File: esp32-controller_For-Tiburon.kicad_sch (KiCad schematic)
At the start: 6 parts, among them J1 Conn_01x02_Pin, J2 Conn_01x02_Pin, J3 SD_Card_Receptacle, J5 Conn_01x04_Pin, J6 Conn_01x02_Pin, U1 ESP32-S3-WROOM-1

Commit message: test push
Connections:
- net at U1.14 (USB_D+): now also J2.1 (Pin_1)
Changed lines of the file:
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@@
 	(generator_version "9.0")
 	(paper "A4")
+	(wire
+		(pts
+			(xy 171.45 87.63) (xy 156.21 87.63)
+		)
+		(stroke
+			(width 0)
+			(type default)
+		)
+	)
+	(wire
+		(pts
+			(xy 171.45 99.06) (xy 171.45 87.63)
+		)
+		(stroke
+			(width 0)
+			(type default)
+		)
+	)
 	(symbol
 		(lib_id "Connector:Conn_01x02_Pin")

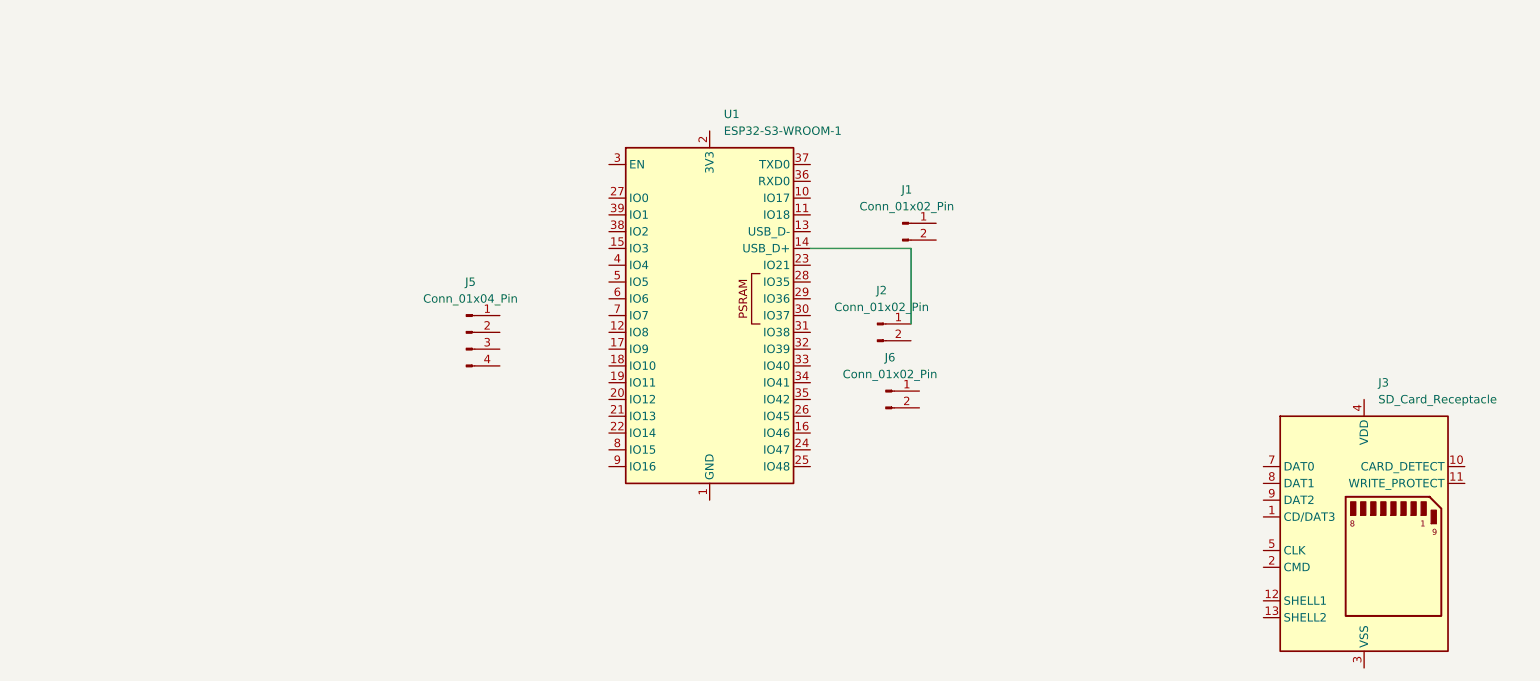
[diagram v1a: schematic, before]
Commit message: added power pin
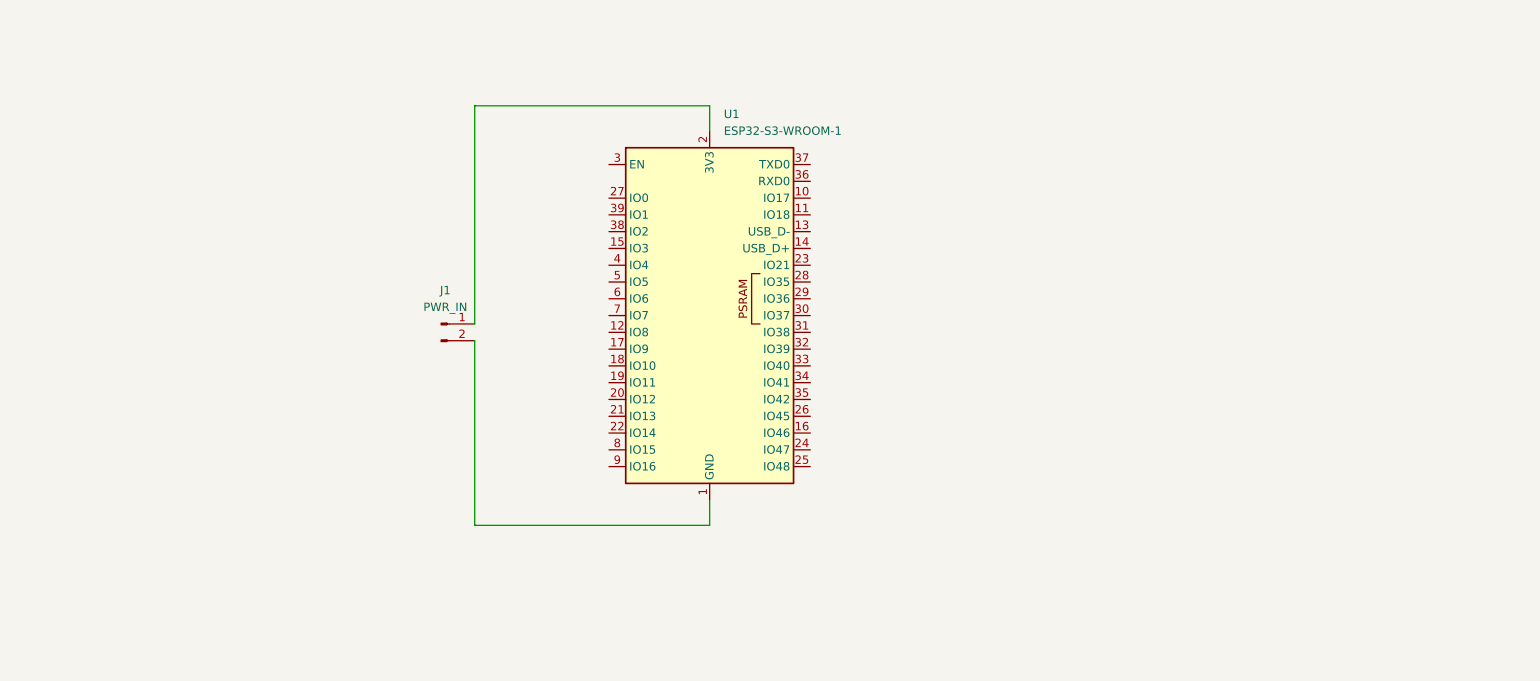
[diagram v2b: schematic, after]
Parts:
- removed J2, J6: Conn_01x02_Pin, symbol Connector:Conn_01x02_Pin
- removed J3: SD_Card_Receptacle, symbol Connector:SD_Card_Receptacle
- removed J5: Conn_01x04_Pin, symbol Connector:Conn_01x04_Pin
- J1: value Conn_01x02_Pin -> PWR_IN
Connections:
- net at J1.1 (Pin_1): now also U1.2 (3V3)
- net at J1.2 (Pin_2): now also U1.1 (GND), U1.40 (GND), U1.41 (GND)

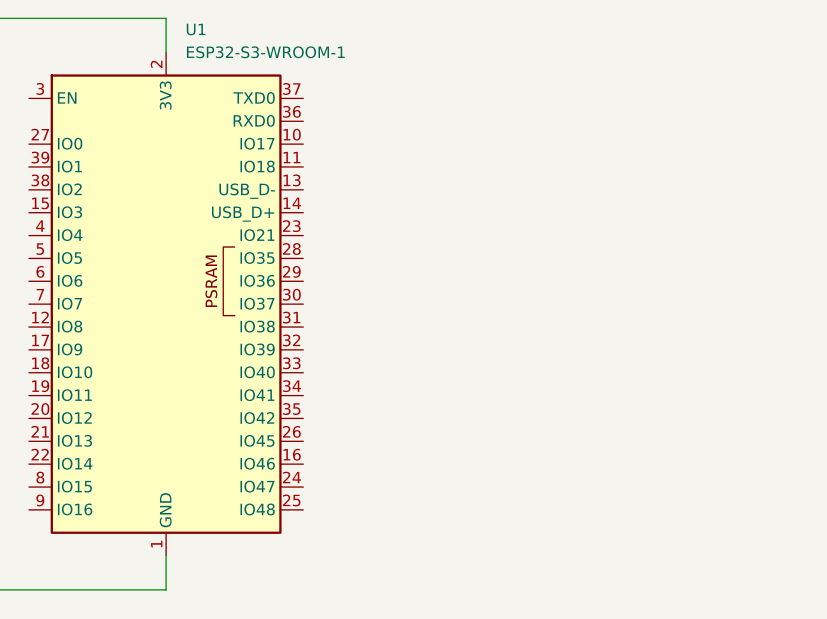
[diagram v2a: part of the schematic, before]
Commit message: added uart pins
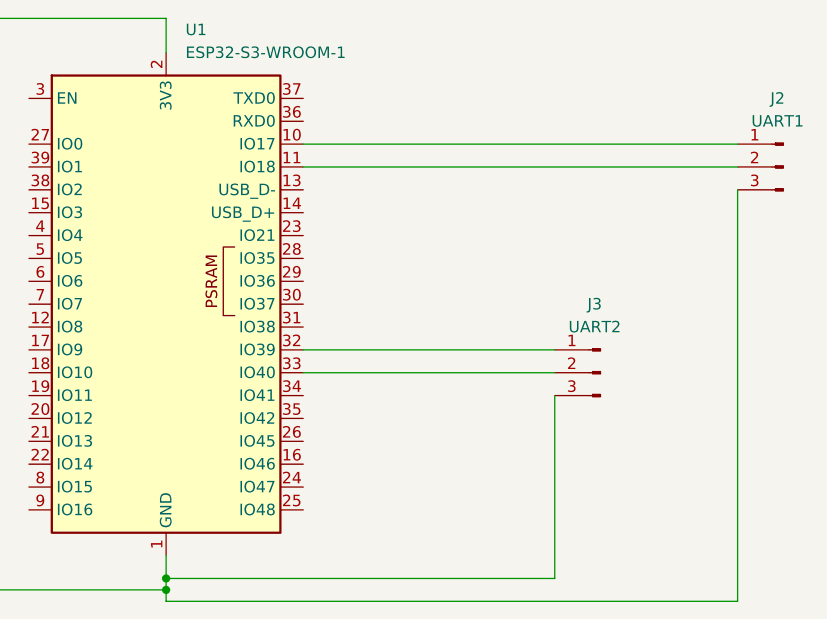
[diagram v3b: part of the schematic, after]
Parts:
- added J2: UART1, symbol Connector:Conn_01x03_Pin
- added J3: UART2, symbol Connector:Conn_01x03_Pin
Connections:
- net at J1.2 (Pin_2), U1.1 (GND), U1.40 (GND)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: now also J2.3 (Pin_3), J3.3 (Pin_3)
- net at U1.10 (IO17): now also J2.1 (Pin_1)
- net at U1.11 (IO18): now also J2.2 (Pin_2)
- net at U1.32 (IO39): now also J3.1 (Pin_1)
- net at U1.33 (IO40): now also J3.2 (Pin_2)
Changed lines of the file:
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@@
 	(generator_version "9.0")
 	(paper "A4")
-	(wire
-		(pts
-			(xy 140.97 129.54) (xy 140.97 125.73)
+	(junction
+		(at 140.97 128.27)
+		(diameter 0)
+		(color 0 0 0 0)
+	)
+	(junction
+		(at 140.97 129.54)
+		(diameter 0)
+		(color 0 0 0 0)
+	)
+	(wire
+		(pts
+			(xy 204.47 85.09) (xy 204.47 130.81)
+		)
+		(stroke
+			(width 0)
+			(type default)
+		)
+	)
+	(wire
+		(pts
+			(xy 140.97 125.73) (xy 140.97 128.27)
 		)
 		(stroke
@@
 	(wire
 		(pts
+			(xy 204.47 130.81) (xy 140.97 130.81)
+		)
+		(stroke
+			(width 0)
+			(type default)
+		)
+	)
+	(wire
+		(pts
 			(xy 105.41 66.04) (xy 140.97 66.04)
 		)
@@
 	(wire
 		(pts
+			(xy 140.97 128.27) (xy 140.97 129.54)
+		)
+		(stroke
+			(width 0)
+			(type default)
+		)
+	)
+	(wire
+		(pts
+			(xy 156.21 80.01) (xy 204.47 80.01)
+		)
+		(stroke
+			(width 0)
+			(type default)
+		)
+	)
+	(wire
+		(pts
+			(xy 184.15 128.27) (xy 140.97 128.27)
+		)
+		(stroke
+			(width 0)
+			(type default)
+		)
+	)
+	(wire
+		(pts
+			(xy 184.15 107.95) (xy 184.15 128.27)
+		)
+		(stroke
+			(width 0)
+			(type default)
+		)
+	)
+	(wire
+		(pts
+			(xy 156.21 82.55) (xy 204.47 82.55)
+		)
+		(stroke
+			(width 0)
+			(type default)
+		)
+	)
+	(wire
+		(pts
 			(xy 105.41 101.6) (xy 105.41 129.54)
+		)
+		(stroke
+			(width 0)
+			(type default)
+		)
+	)
+	(wire
+		(pts
+			(xy 140.97 129.54) (xy 140.97 130.81)
+		)
+		(stroke
+			(width 0)
+			(type default)
+		)
+	)
+	(wire
+		(pts
+			(xy 156.21 102.87) (xy 184.15 102.87)
+		)
+		(stroke
+			(width 0)
+			(type default)
+		)
+	)
+	(wire
+		(pts
+			(xy 156.21 105.41) (xy 184.15 105.41)
 		)
 		(stroke
@@
 					(unit 1)
 				)
+			)
+		)
+	)
+	(symbol
+		(lib_id "Connector:Conn_01x03_Pin")
+		(at 189.23 105.41 0)
+		(mirror y)
+		(unit 1)
+		(exclude_from_sim no)
+		(in_bom yes)
+		(on_board yes)
+		(dnp no)
+		(property "Reference" "J3"
+			(at 188.595 97.79 0)
+			(effects
+				(font
+					(size 1.27 1.27)
+				)
+			)
+		)
+		(property "Value" "UART2"
+			(at 188.595 100.33 0)
+			(effects
+				(font
+					(size 1.27 1.27)
+				)
+			)
+		)
+		(property "Footprint" ""
+			(at 189.23 105.41 0)
+			(effects
+				(font
+					(size 1.27 1.27)
+				)
+				(hide yes)
+			)
+		)
+		(property "Datasheet" "~"
+			(at 189.23 105.41 0)
+			(effects
+				(font
+					(size 1.27 1.27)
+				)
+				(hide yes)
+			)
+		)
+		(property "Description" "Generic connector, single row, 01x03, script generated"
+			(at 189.23 105.41 0)
+			(effects
+				(font
+					(size 1.27 1.27)
+				)
+				(hide yes)
+			)
+		)
+		(pin "1"
+		)
+		(pin "2"
+		)
+		(pin "3"
+		)
+		(instances
+			(project "esp32-controller_For-Tiburon"
+				(path "/eae6b2b7-7c39-475f-a588-61e077f8b686"
+					(reference "J3")
+					(unit 1)
+				)
+			)
+		)
+	)
+	(symbol
+		(lib_id "Connector:Conn_01x03_Pin")
+		(at 209.55 82.55 0)
+		(mirror y)
+		(unit 1)
+		(exclude_from_sim no)
+		(in_bom yes)
+		(on_board yes)
+		(dnp no)
+		(property "Reference" "J2"
+			(at 208.915 74.93 0)
+			(effects
+				(font
+					(size 1.27 1.27)
+				)
+			)
+		)
+		(property "Value" "UART1"
+			(at 208.915 77.47 0)
+			(effects
+				(font
+					(size 1.27 1.27)
+				)
+			)
+		)
+		(property "Footprint" ""
+			(at 209.55 82.55 0)
+			(effects
+				(font
+					(size 1.27 1.27)
+				)
+				(hide yes)
+			)
+		)
+		(property "Datasheet" "~"
+			(at 209.55 82.55 0)
+			(effects
+				(font
+					(size 1.27 1.27)
+				)
+				(hide yes)
+			)
+		)
+		(property "Description" "Generic connector, single row, 01x03, script generated"
+			(at 209.55 82.55 0)
+			(effects
+				(font
+					(size 1.27 1.27)
+				)
+				(hide yes)
+			)
+		)
+		(pin "1"
+		)
+		(pin "2"
+		)
+		(pin "3"
+		)
+		(instances
+			(project ""
+				(path "/eae6b2b7-7c39-475f-a588-61e077f8b686"
+					(reference "J2")
+					(unit 1)
+				)

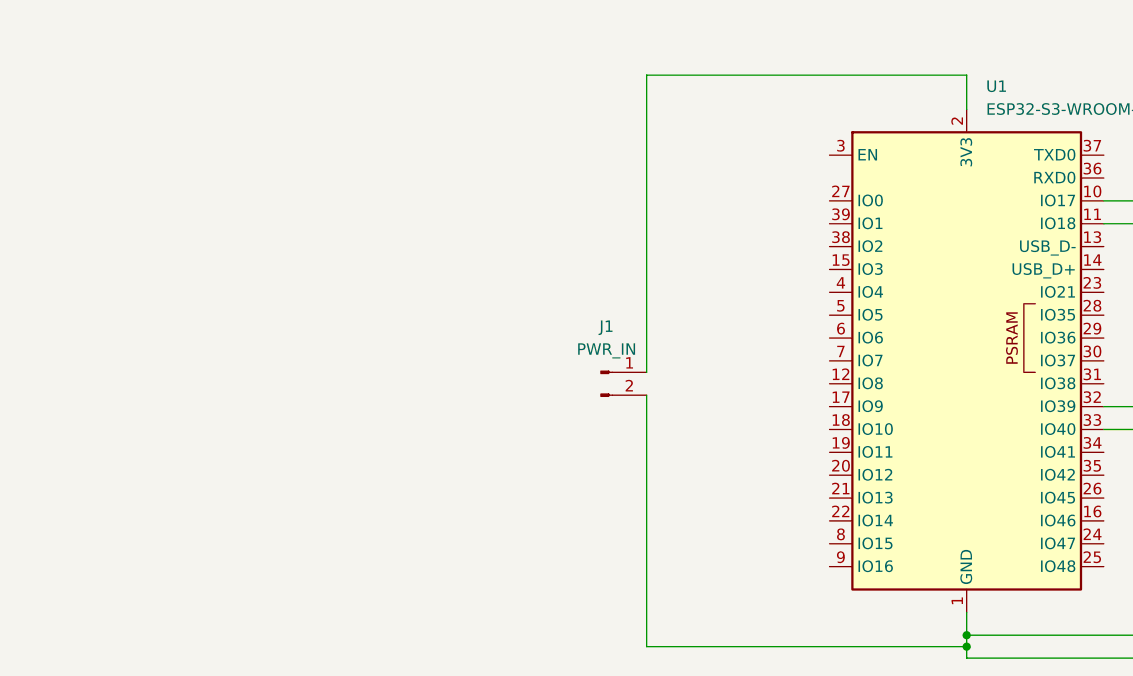
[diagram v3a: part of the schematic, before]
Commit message: added 12c pins
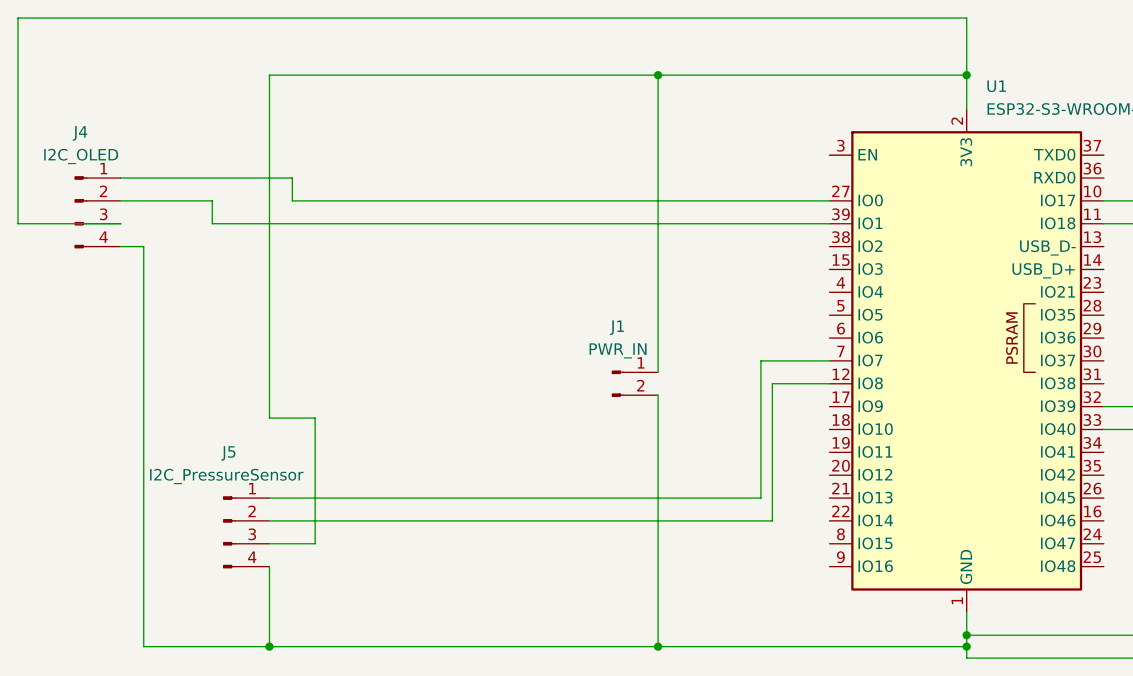
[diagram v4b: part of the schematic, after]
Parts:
- added J4: I2C_OLED, symbol Connector:Conn_01x04_Pin
- added J5: I2C_PressureSensor, symbol Connector:Conn_01x04_Pin
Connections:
- net at J1.1 (Pin_1), U1.2 (3V3): now also J4.3 (Pin_3), J5.3 (Pin_3)
- net at J1.2 (Pin_2), J2.3 (Pin_3), J3.3 (Pin_3)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: now also J4.4 (Pin_4), J5.4 (Pin_4)
- net at U1.12 (IO8): now also J5.2 (Pin_2)
- net at U1.27 (IO0): now also J4.1 (Pin_1)
- net at U1.39 (IO1): now also J4.2 (Pin_2)
- net at U1.7 (IO7): now also J5.1 (Pin_1)
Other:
- moved on the sheet: J1

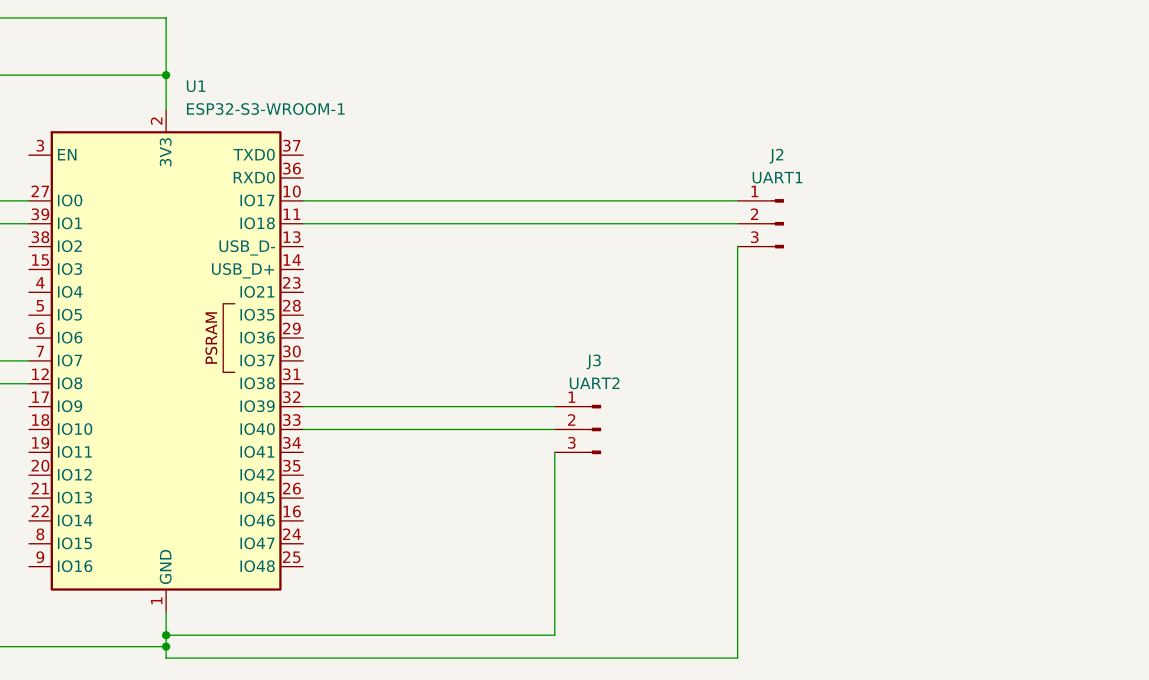
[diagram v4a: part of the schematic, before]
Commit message: added sd card
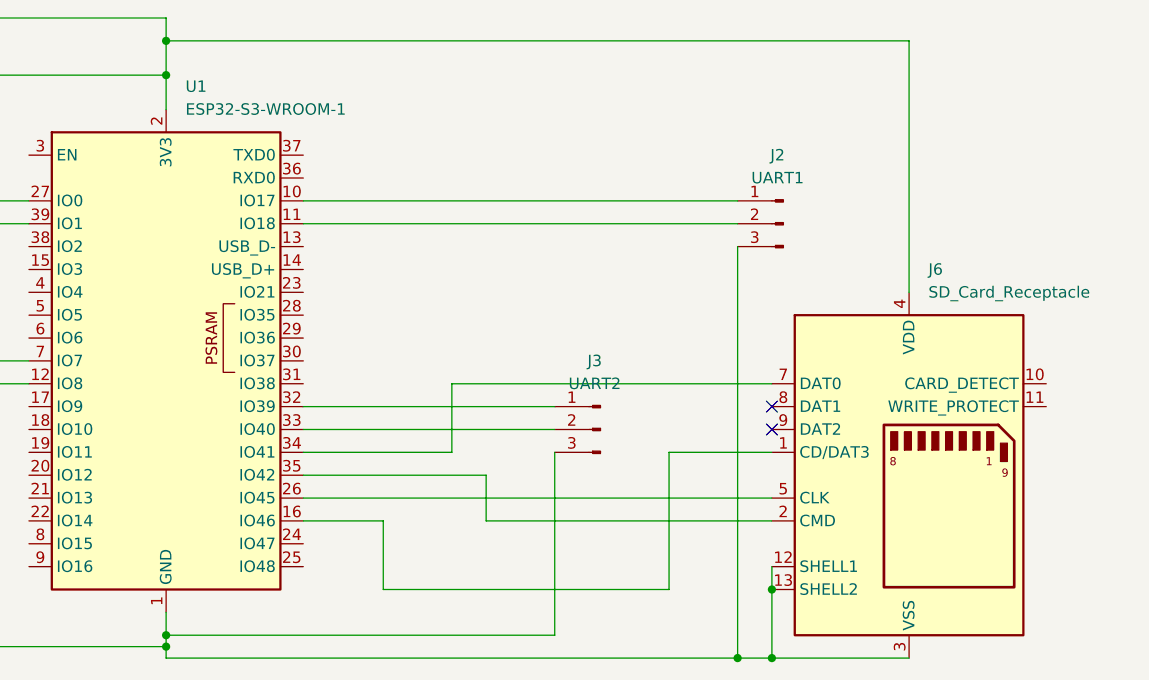
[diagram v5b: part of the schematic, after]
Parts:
- added J6: SD_Card_Receptacle, symbol Connector:SD_Card_Receptacle
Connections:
- net at J1.1 (Pin_1), J4.3 (Pin_3), J5.3 (Pin_3)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: now also J6.4 (VDD)
- net at J1.2 (Pin_2), J2.3 (Pin_3), J3.3 (Pin_3)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: now also J6.12 (SHELL1), J6.13 (SHELL2), J6.3 (VSS), J6.6 (VSS)
- net at U1.16 (IO46): now also J6.1 (CD/DAT3)
- net at U1.26 (IO45): now also J6.5 (CLK)
- net at U1.34 (IO41): now also J6.7 (DAT0)
- net at U1.35 (IO42): now also J6.2 (CMD)
- no-connect marks 0 -> 2
